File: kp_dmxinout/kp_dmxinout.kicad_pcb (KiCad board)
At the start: 2 copper layers, 9 parts, among them J1 NC3MAAH, J2 NC3FAAH, J3 Conn_01x04, U1 SN75176AD, U2 6N137, U3 6N137, U4 SN75176AD

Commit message: fix drc errors
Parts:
- moved PS1 8.37 mm to (182.2, 70.0)
- moved J3 5.74 mm to (191.7, 70.0)
- moved U2 5.51 mm to (141.0, 67.2)
- moved U4 4.17 mm to (165.0, 70.8), turned to -90 degrees
- moved U1 3.83 mm to (165.1, 62.3), turned to 90 degrees
- moved U3 2.61 mm to (144.0, 52.8)

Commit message: dmxinout: do board
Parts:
- added C1: 4.7u, Capacitor_SMD:C_1206_3216Metric, B.Cu at (190.9, 66.9)
- added C2: 10u, Capacitor_SMD:C_1206_3216Metric, B.Cu at (190.9, 61.7)
- added C3: 100n, Capacitor_SMD:C_0402_1005Metric, F.Cu at (180.8, 59.3)
- added C4: 100n, Capacitor_SMD:C_0402_1005Metric, B.Cu at (167.9, 55.3)
- added C5: 100n, Capacitor_SMD:C_0402_1005Metric, F.Cu at (173.2, 77.5)
- added C6: 100n, Capacitor_SMD:C_0402_1005Metric, B.Cu at (182.2, 72.2)
- added C7: 1u, Capacitor_SMD:C_1206_3216Metric, B.Cu at (172.7, 47.6)
- added C8: 1u, Capacitor_SMD:C_1206_3216Metric, B.Cu at (172.1, 84.8)
- added R1: 470, Resistor_SMD:R_0603_1608Metric, B.Cu at (168.1, 64.9)
- added R2: 3000, Resistor_SMD:R_0603_1608Metric, F.Cu at (180.8, 63.6)
- added R3: 470, Resistor_SMD:R_0603_1608Metric, B.Cu at (190.2, 81.6)
- added R4: 3000, Resistor_SMD:R_0603_1608Metric, B.Cu at (191.6, 76.4)
- added R5: 3000, Resistor_SMD:R_0603_1608Metric, F.Cu at (178.1, 75.0)
- added R6: 120, Resistor_SMD:R_0603_1608Metric, B.Cu at (165.6, 84.8)
- added R7: 120, Resistor_SMD:R_0603_1608Metric, B.Cu at (165.4, 48.8)
- J3: footprint Connector_JST:JST_XH_B4B-XH-A_1x04_P2.50mm_Vertical -> Connector_IDC:IDC-Header_2x03_P2.54mm_Vertical
- U1, U3: moved to B.Cu
- moved U3 52.3 mm to (189.4, 78.9), turned to 135 degrees
- moved G*** 46.4 mm to (152.1, 64.1), turned to -90 degrees
- moved U2 31.2 mm to (171.2, 59.2)
- moved U4 7.54 mm to (172.1, 73.3), turned to -135 degrees
- moved J2 6.28 mm to (167.7, 88.0), turned to -135 degrees
- moved PS1 6.02 mm to (187.9, 68.1)
- moved J3 5.82 mm to (197.1, 68.0)
- moved J1 2.83 mm to (171.2, 51.5)
- moved U1 2.53 mm to (165.5, 59.8)
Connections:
- net IN_DATAMINUS renamed IN_DATA-
- net IN_DATAPLUS renamed IN_DATA+
- net OUT_DATAMINUS renamed OUT_DATA-
- net OUT_DATAPLUS renamed OUT_DATA+
- J1 pad 1: Earth -> IN_SHIELD
- J1 pad G: Earth -> unconnected-(J1-PadG)
- J2 pad 1: Earth -> OUT_SHIELD
- U2 pad 3: Net-(U2-C) -> /6n137_in_c
- U3 pad 3: Net-(U3-C) -> /6n137_out_c
- U3 pad 6: IN_DATATTL -> OUT_DATATTL
- U4 pad 4: IN_DATATTL -> OUT_DATATTL
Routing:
- net +5V: track 0.00 -> 83.2 mm, vias 0 -> 1
- net +5V_IN: track 0.00 -> 50.9 mm
- net MCU_DMX_IN: track 0.00 -> 26.7 mm
- net MCU_DMX_OUT: track 0.00 -> 22.0 mm
- net GND_IN: track 0.00 -> 20.6 mm, vias 0 -> 3
- net OUT_DATATTL: track 0.00 -> 15.0 mm
- net OUT_DATA+: track 0.00 -> 14.7 mm
- net OUT_DATA-: track 0.00 -> 14.5 mm
- net IN_DATA-: track 0.00 -> 9.87 mm
- net IN_DATA+: track 0.00 -> 9.84 mm
- net OUT_SHIELD: track 0.00 -> 4.22 mm
- net /6n137_out_c: track 0.00 -> 4.02 mm
- net IN_SHIELD: track 0.00 -> 3.82 mm
- net GND: track 0.00 -> 3.05 mm, vias 0 -> 20
- net IN_DATATTL: track 0.00 -> 2.69 mm
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- added copper zone on B.Cu, net GND
- added copper zone on F.Cu, net GND
- added copper zone on B.Cu, net GND_IN
- added copper zone on F.Cu, net GND_IN
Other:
- board outline added: 63.1 x 63.1 mm

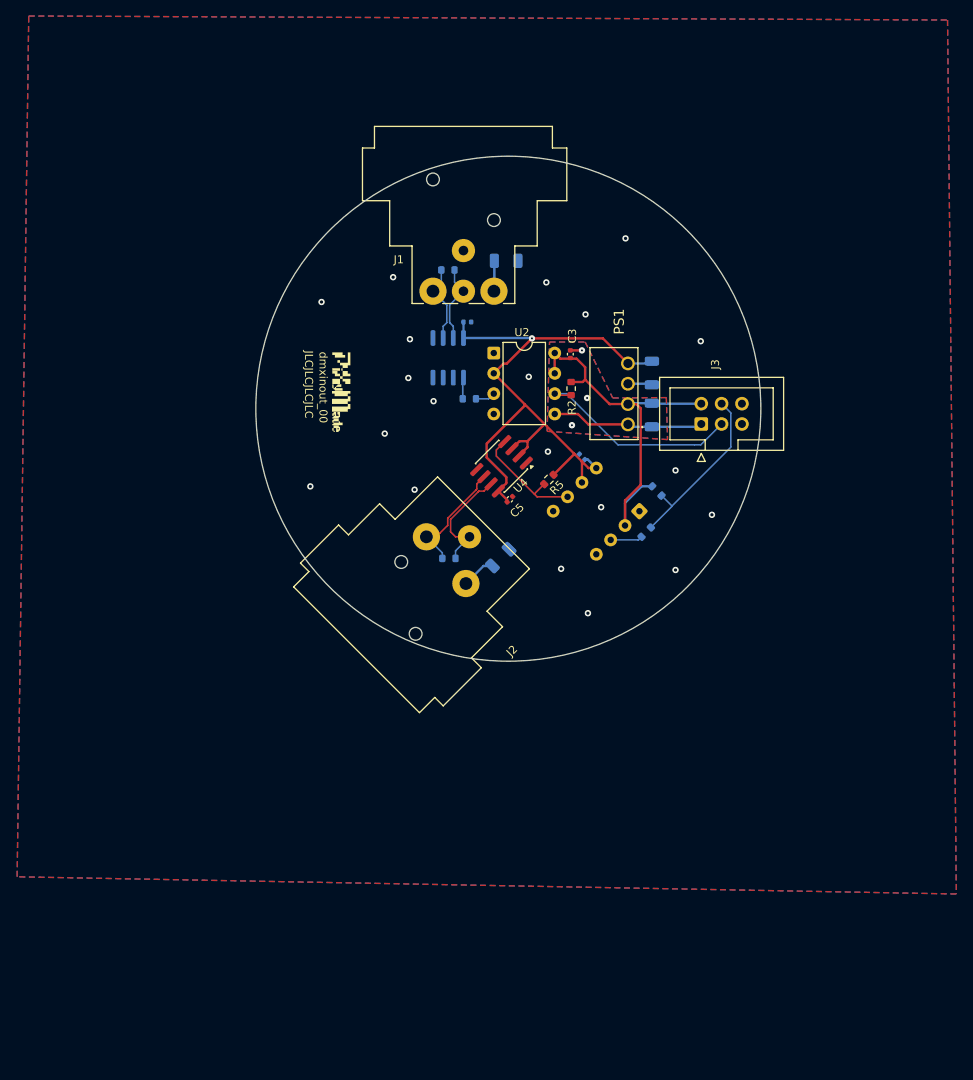
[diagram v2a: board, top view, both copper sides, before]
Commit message: dmx: disconnect shield & gnd
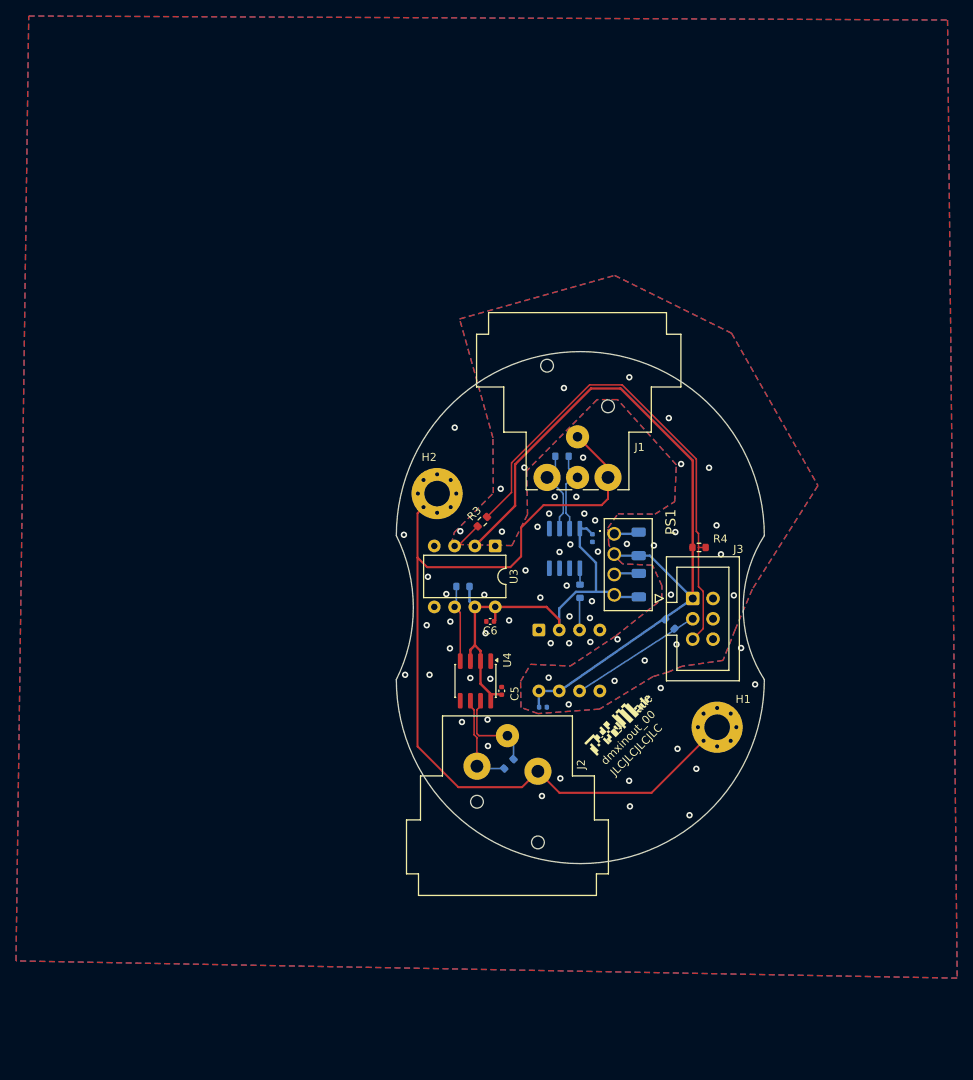
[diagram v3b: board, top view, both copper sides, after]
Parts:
- removed C7, C8: 1u, Capacitor_SMD:C_1206_3216Metric
- added H1: MountingHole_Pad, MountingHole:MountingHole_3.2mm_M3_Pad_Via, F.Cu at (199.1, 106.0)
- added H2: MountingHole_Pad, MountingHole:MountingHole_3.2mm_M3_Pad_Via, F.Cu at (164.1, 76.7)
- C3, R2, R5, U2: moved to B.Cu
- C6, R3, R4, U3: moved to F.Cu
- moved G*** 53.8 mm to (186.8, 105.2), turned to 45 degrees
- moved C3 44.3 mm to (177.3, 103.5), turned to 0 degrees
- moved U2 35.1 mm to (176.8, 93.8), turned to -90 degrees
- moved R2 31.9 mm to (193.2, 93.1), turned to -45 degrees
- moved C4 31.2 mm to (183.5, 82.3), turned to -90 degrees
- moved U1 27.9 mm to (180.0, 83.6)
- moved R1 27.7 mm to (182.0, 89.0), turned to -90 degrees
- moved J1 27.3 mm to (185.5, 74.7)
- moved R7 27.3 mm to (179.7, 72.1)
- moved U4 27.0 mm to (168.9, 100.2), turned to -90 degrees
- moved R6 26.8 mm to (173.1, 110.5), turned to 45 degrees
- moved C2 26.6 mm to (189.3, 88.2), turned to 90 degrees
- moved J2 25.1 mm to (176.7, 111.5), turned to -90 degrees
- moved C5 24.0 mm to (172.2, 101.4), turned to 90 degrees
- moved C6 23.6 mm to (170.7, 92.7), turned to 180 degrees
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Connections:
- J1 pad 1: IN_SHIELD -> SHIELD
- J1 pad G: unconnected-(J1-PadG) -> SHIELD
- J2 pad 1: OUT_SHIELD -> SHIELD
- J3 pad 1: GND_IN -> +5V_IN
- J3 pad 2: +5V_IN -> GND_IN
- J3 pad 4: MCU_DMX_OUT -> GND_IN
- J3 pad 5: unconnected-(J3-Pin_5-Pad5) -> MCU_DMX_OUT
- J3 pad 6: unconnected-(J3-Pin_6-Pad6) -> GND_IN
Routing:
- net SHIELD: track 0.00 -> 116.8 mm
- net MCU_DMX_OUT: track 22.0 -> 63.3 mm
- net +5V: track 83.2 -> 56.3 mm, vias 1 -> 0
- net MCU_DMX_IN: track 26.7 -> 0.17 mm
- net +5V_IN: track 50.9 -> 76.5 mm
- net GND_IN: track 20.6 -> 3.14 mm, vias 3 -> 22
- net OUT_DATATTL: track 15.0 -> 9.72 mm
- net OUT_SHIELD: track 4.22 -> 0.00 mm
- net IN_SHIELD: track 3.82 -> 0.00 mm
- net OUT_DATA-: track 14.5 -> 11.5 mm
- net OUT_DATA+: track 14.7 -> 12.0 mm
- net /6n137_in_c: track 2.50 -> 4.04 mm
- net IN_DATA-: track 9.87 -> 10.6 mm
- net IN_DATA+: track 9.84 -> 10.5 mm
- net IN_DATATTL: track 2.69 -> 2.06 mm
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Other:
- board size 63.1 x 63.1 mm -> 46 x 64 mm

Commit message: main board : start doing sig gnd gnd sigpow
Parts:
- moved R2 6.16 mm to (189.4, 98.0), turned to 135 degrees
- moved J3 6.05 mm to (198.8, 95.2), turned to 180 degrees
- moved R7 0.37 mm to (179.7, 72.5)
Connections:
- J3 pad 1: +5V_IN -> GND_IN
- J3 pad 2: GND_IN -> +5V_IN
- J3 pad 3: MCU_DMX_IN -> GND_IN
- J3 pad 4: GND_IN -> MCU_DMX_IN
- J3 pad 5: MCU_DMX_OUT -> GND_IN
- J3 pad 6: GND_IN -> MCU_DMX_OUT
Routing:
- net +5V_IN: track 76.5 -> 90.0 mm, vias 0 -> 1
- net GND_IN: track 3.14 -> 8.22 mm, vias 22 -> 30
- net MCU_DMX_OUT: track 63.3 -> 58.4 mm
- net GND: vias 46 -> 50

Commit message: DRC OK
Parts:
- moved G*** 8.57 mm to (191.1, 112.6)
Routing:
- net SHIELD: track 116.8 -> 0.00 mm
- net GND: vias 50 -> 27
- added copper zone on B.Cu, net SHIELD
- added copper zone on F.Cu, net SHIELD

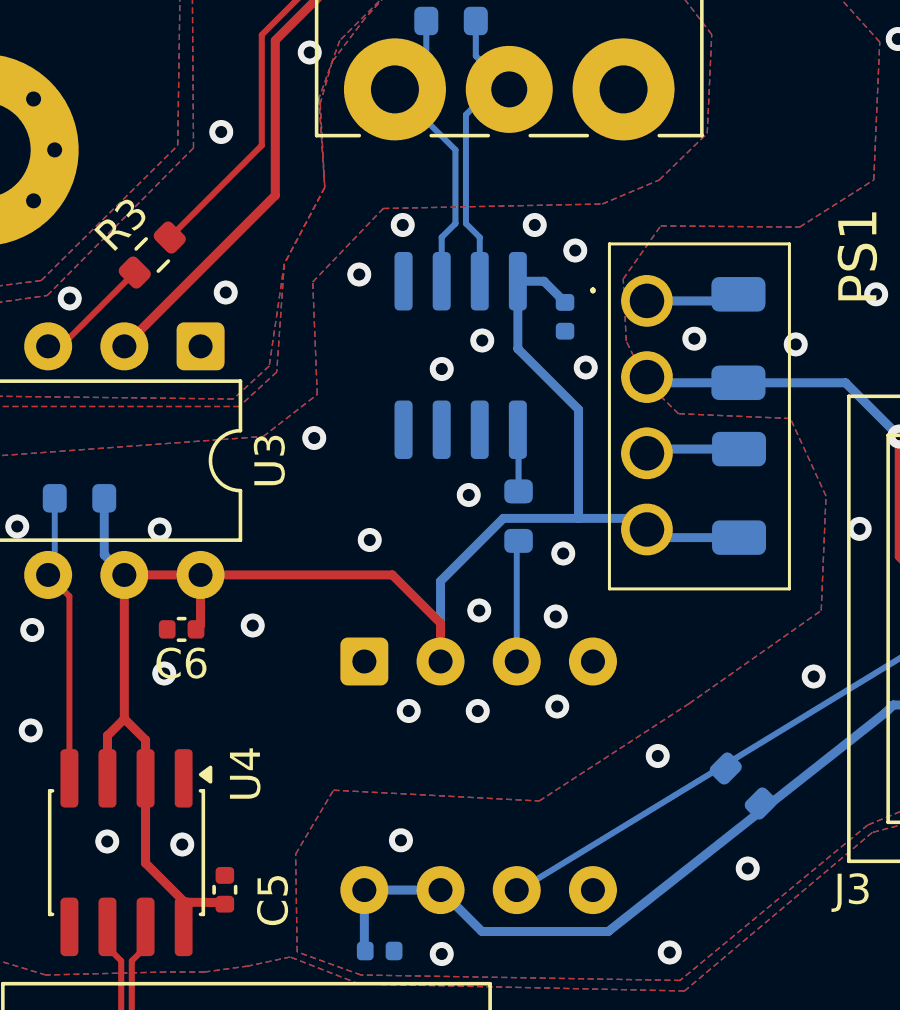
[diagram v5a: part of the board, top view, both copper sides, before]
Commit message: add pwr leds
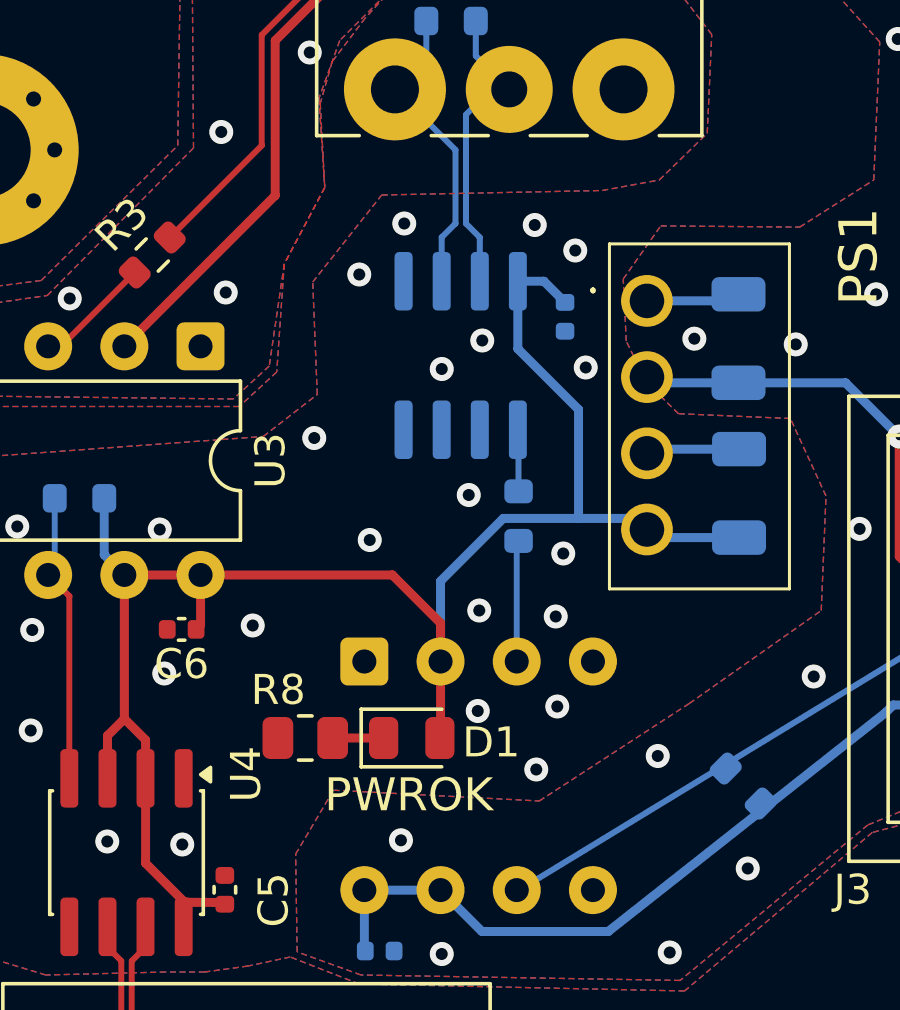
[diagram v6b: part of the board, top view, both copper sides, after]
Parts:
- added D1: LED, LED_SMD:LED_0805_2012Metric, F.Cu at (178.4, 96.3)
- added R8: 3k, Resistor_SMD:R_0805_2012Metric, F.Cu at (174.8, 96.3)
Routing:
- net +5V: track 56.3 -> 58.9 mm
- net /led: track 0.00 -> 1.70 mm
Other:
- board text added: "PWROK"

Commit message: ready 4 prod
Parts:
- R2, R4, R5: value 3000 -> 3k; footprint Resistor_SMD:R_0603_1608Metric -> Resistor_SMD:R_0805_2012Metric
- moved R4 0.10 mm to (196.7, 83.5)
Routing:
- net MCU_DMX_OUT: track 58.4 -> 59.2 mm
